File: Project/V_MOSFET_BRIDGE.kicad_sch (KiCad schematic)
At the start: 14 parts, among them Q401 DMT68M8LFV-7, Q402 DMT68M8LFV-7

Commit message: More files cleanup
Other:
- company: Quasi Peak -> ${COMPANY}

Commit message: Cleanup ED A1 version
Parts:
- C403: symbol Device:CP -> Device:C_Polarized
- Q401, Q402: symbol eval_board_tmc6200-ta:DMT68M8LFV-7 -> QP_LIBRARY:DMT68M8LFV-7

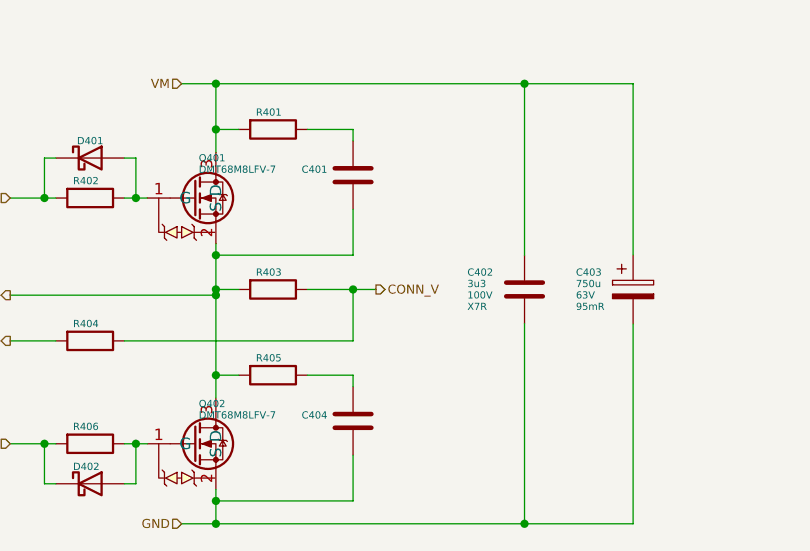
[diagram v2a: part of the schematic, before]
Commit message: Cleaning files, added testpoints
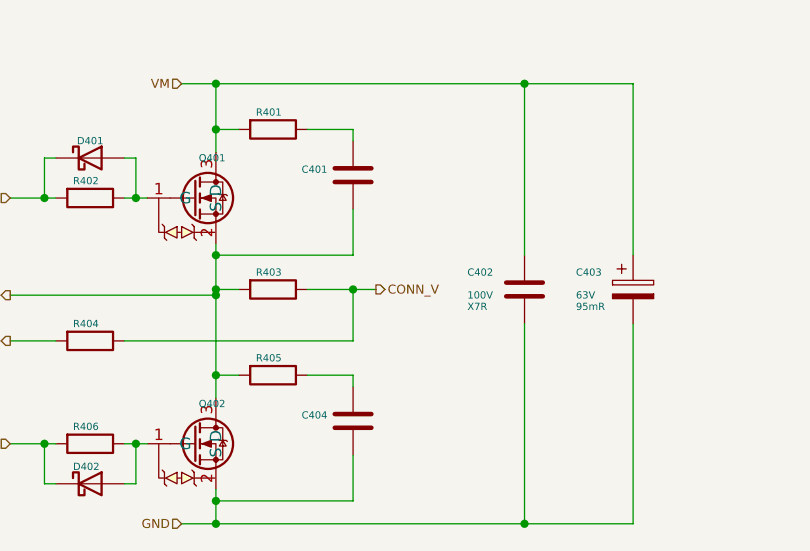
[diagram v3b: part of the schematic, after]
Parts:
- C401, C404: value C -> ~; footprint Capacitor_SMD:C_0402_1005Metric -> (none)
- C402: value 3u3 -> ~; footprint Capacitor_SMD:C_1812_4532Metric -> (none)
- C403: value 750u -> ~; footprint Capacitor_SMD:CP_Elec_18x17.5 -> (none)
- D401, D402: value D_Schottky -> ~; footprint Diode_SMD:D_SOD-123 -> (none)
- Q401, Q402: value DMT68M8LFV-7 -> ~; footprint eval_board_tmc6200-ta:DMT68M8LFV-7_PowerDI5060-8 -> (none)
- R401, R402, R404, R405, R406: value R -> ~; footprint Resistor_SMD:R_0402_1005Metric -> (none)
- R403: value R -> ~; footprint Resistor_SMD:R_1210_3225Metric -> (none)
